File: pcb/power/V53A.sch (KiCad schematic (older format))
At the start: 7 parts

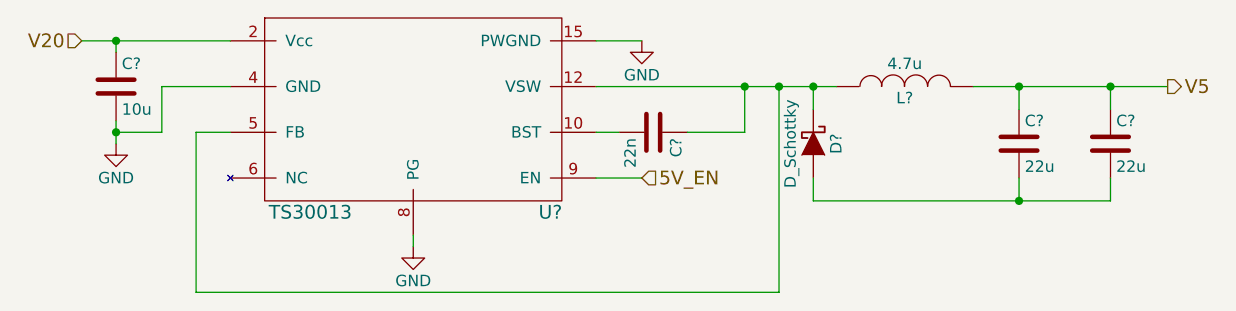
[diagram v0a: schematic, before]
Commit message: Finished almost everything in the schematic. Missing: Interfacing with elmare and the correct power connector for the 20 V power supply.
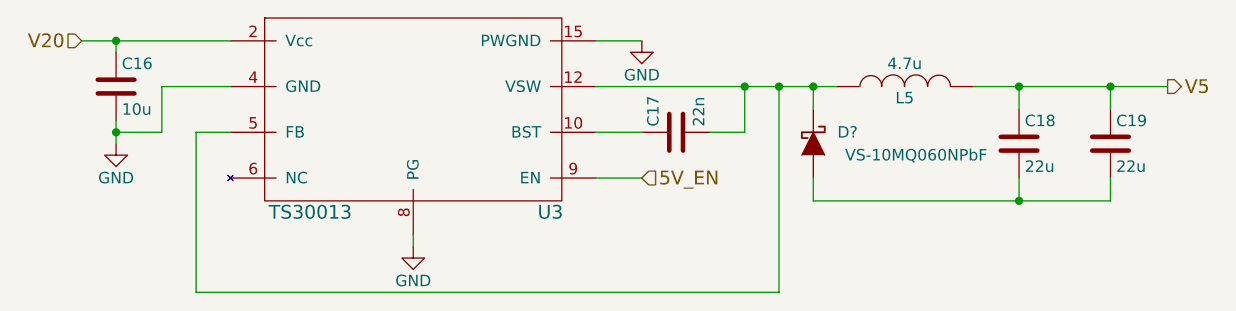
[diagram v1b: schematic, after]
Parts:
- removed C?: 10u, symbol C
- removed C?: 22u, symbol C
- removed C?: 22n, symbol C
- removed D?: D_Schottky, symbol D_Schottky
- added C16: 10u, symbol C
- added C17: 22n, symbol C
- added C19: 22u, symbol C
- added D?: VS-10MQ060NPbF, symbol D_Schottky
- C18: renamed from C?; Digikey (none) -> 1276-1193-1-ND
- L5: renamed from L?; Digikey (none) -> 587-2969-1-ND
- U3: renamed from U?; Digikey (none) -> TS30013-M050QFNRCT-ND
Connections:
- net GND: now also C16.2
- net V20: now also C16.1
- net V5: now also C19.1
- net at L5.1, U3.1 (VSW), U3.12 (VSW)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: now also C17.2, D?.1 (K)
- net at U3.10 (BST): now also C17.1
- net at C18.2: now also C19.2, D?.2 (A)
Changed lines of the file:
@@
 $EndDescr
 $Comp
-L TS30013 U?
+L TS30013 U3
 U 1 1 583B345B
 P 4450 3200
-F 0 "U?" H 5100 2750 60  0000 C CNN
+F 0 "U3" H 5100 2750 60  0000 C CNN
 F 1 "TS30013" H 4050 2750 60  0000 C CNN
 F 2 "" H 4550 3200 60  0000 C CNN
-F 3 "" H 4550 3200 60  0000 C CNN
+F 3 "http://www.semtech.com/images/datasheet/ts30011_12_13.pdf" H 4550 3200 60  0001 C CNN
+F 4 "TS30013-M050QFNRCT-ND" H 4450 3200 60  0001 C CNN "Digikey"
 	1    4450 3200
 	1    0    0    -1
 $EndComp
 $Comp
-L GND #PWR?
+L GND #PWR12
 U 1 1 583B3462
 P 5500 2900
-F 0 "#PWR?" H 5500 2650 50  0001 C CNN
+F 0 "#PWR12" H 5500 2650 50  0001 C CNN
 F 1 "GND" H 5500 2750 50  0000 C CNN
 F 2 "" H 5500 2900 50  0000 C CNN
@@
 $EndComp
 $Comp
-L GND #PWR?
+L GND #PWR10
 U 1 1 583B3468
 P 3200 3350
-F 0 "#PWR?" H 3200 3100 50  0001 C CNN
+F 0 "#PWR10" H 3200 3100 50  0001 C CNN
 F 1 "GND" H 3200 3200 50  0000 C CNN
 F 2 "" H 3200 3350 50  0000 C CNN
@@
 $EndComp
 $Comp
-L C C?
-U 1 1 583B346F
-P 3200 3100
-F 0 "C?" H 3225 3200 50  0000 L CNN
-F 1 "10u" H 3225 3000 50  0000 L CNN
-F 2 "" H 3238 2950 50  0000 C CNN
-F 3 "" H 3200 3100 50  0000 C CNN
-	1    3200 3100
-	1    0    0    -1
-$EndComp
-$Comp
-L C C?
+L C C18
 U 1 1 583B3476
 P 7150 3350
-F 0 "C?" H 7175 3450 50  0000 L CNN
+F 0 "C18" H 7175 3450 50  0000 L CNN
 F 1 "22u" H 7175 3250 50  0000 L CNN
 F 2 "" H 7188 3200 50  0000 C CNN
-F 3 "" H 7150 3350 50  0000 C CNN
+F 3 "http://www.samsungsem.com/kr/support/product-search/mlcc/__icsFiles/afieldfile/2016/08/18/S_CL10A226MQ8NRNC.pdf" H 7150 3350 50  0001 C CNN
+F 4 "1276-1193-1-ND" H 7150 3350 60  0001 C CNN "Digikey"
 	1    7150 3350
 	1    0    0    -1
 $EndComp
 $Comp
-L C C?
-U 1 1 583B347D
-P 7550 3350
-F 0 "C?" H 7575 3450 50  0000 L CNN
-F 1 "22u" H 7575 3250 50  0000 L CNN
-F 2 "" H 7588 3200 50  0000 C CNN
-F 3 "" H 7550 3350 50  0000 C CNN
-	1    7550 3350
-	1    0    0    -1
-$EndComp
-$Comp
-L INDUCTOR L?
+L INDUCTOR L5
 U 1 1 583B3484
 P 6650 3100
-F 0 "L?" V 6600 3100 50  0000 C CNN
+F 0 "L5" V 6600 3100 50  0000 C CNN
 F 1 "4.7u" V 6750 3100 50  0000 C CNN
 F 2 "" H 6650 3100 50  0000 C CNN
-F 3 "" H 6650 3100 50  0000 C CNN
+F 3 "http://www.yuden.co.jp/productdata/catalog/en/wound04_e.pdf" H 6650 3100 50  0001 C CNN
+F 4 "587-2969-1-ND " V 6650 3100 60  0001 C CNN "Digikey"
 	1    6650 3100
 	0    -1   -1   0
 $EndComp
 $Comp
-L D_Schottky D?
-U 1 1 583B348B
-P 6250 3350
-F 0 "D?" H 6250 3450 50  0000 C CNN
-F 1 "D_Schottky" H 6250 3250 50  0000 C CNN
-F 2 "" H 6250 3350 50  0000 C CNN
-F 3 "" H 6250 3350 50  0000 C CNN
-	1    6250 3350
-	0    1    1    0
-$EndComp
-$Comp
-L GND #PWR?
+L GND #PWR11
 U 1 1 583B3492
 P 4500 3800
-F 0 "#PWR?" H 4500 3550 50  0001 C CNN
+F 0 "#PWR11" H 4500 3550 50  0001 C CNN
 F 1 "GND" H 4500 3650 50  0000 C CNN
 F 2 "" H 4500 3800 50  0000 C CNN
@@
 	1    4500 3800
 	1    0    0    -1
-$EndComp
-$Comp
-L C C?
-U 1 1 583B3498
-P 5550 3300
-F 0 "C?" H 5575 3400 50  0000 L CNN
-F 1 "22n" H 5575 3200 50  0000 L CNN
-F 2 "" H 5588 3150 50  0000 C CNN
-F 3 "" H 5550 3300 50  0000 C CNN
-	1    5550 3300
-	0    1    1    0
 $EndComp
 Wire Wire Line
@@
 	5300 2900 5500 2900
 Wire Wire Line
-	5300 3300 5400 3300
-Wire Wire Line
-	5700 3300 5950 3300
+	5300 3300 5500 3300
 Connection ~ 5950 3100
 Wire Wire Line
@@
 Wire Wire Line
 	5500 3500 5300 3500
+$Comp
+L C C16
+U 1 1 583C14BA
+P 3200 3100
+F 0 "C16" H 3225 3200 50  0000 L CNN
+F 1 "10u" H 3225 3000 50  0000 L CNN
+F 2 "" H 3238 2950 50  0000 C CNN
+F 3 "http://search.murata.co.jp/Ceramy/image/img/A01X/G101/ENG/GRT188R61E106ME13-01.pdf" H 3200 3100 50  0001 C CNN
+F 4 "490-12323-1-ND" H 3200 3100 60  0001 C CNN "Digikey"
+	1    3200 3100
+	1    0    0    -1
+$EndComp
+$Comp
+L C C17
+U 1 1 583C19B4
+P 5650 3300
+F 0 "C17" H 5675 3400 50  0000 L CNN
+F 1 "22n" H 5675 3200 50  0000 L CNN
+F 2 "" H 5688 3150 50  0000 C CNN
+F 3 "https://product.tdk.com/info/en/catalog/datasheets/mlcc_highreliability_general_en.pdf" H 5650 3300 50  0001 C CNN
+F 4 "445-8118-1-ND" H 5650 3300 60  0001 C CNN "Digikey"
+	1    5650 3300
+	0    -1   -1   0
+$EndComp
+Wire Wire Line
+	5800 3300 5950 3300
+$Comp
+L C C19
+U 1 1 583C1DEC
+P 7550 3350
+F 0 "C19" H 7575 3450 50  0000 L CNN
+F 1 "22u" H 7575 3250 50  0000 L CNN
+F 2 "" H 7588 3200 50  0000 C CNN
+F 3 "http://www.samsungsem.com/kr/support/product-search/mlcc/__icsFiles/afieldfile/2016/08/18/S_CL10A226MQ8NRNC.pdf" H 7550 3350 50  0001 C CNN
+F 4 "1276-1193-1-ND" H 7550 3350 60  0001 C CNN "Digikey"
+	1    7550 3350
+	1    0    0    -1
+$EndComp
+$Comp
+L D_Schottky D?
+U 1 1 583C3D85
+P 6250 3350
+F 0 "D?" V 6200 3500 50  0000 C CNN
+F 1 "VS-10MQ060NPbF" V 6300 3800 50  0000 C CNN
+F 2 "" H 6250 3350 50  0000 C CNN
+F 3 "http://www.vishay.com/docs/88869/packaging.pdf" H 6250 3350 50  0001 C CNN
+F 4 "10MQ060NPBFCT-ND" V 6300 3950 60  0001 C CNN "Digikey"
+	1    6250 3350
+	0    1    1    0
+$EndComp
 $EndSCHEMATC

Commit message: Almost done with the schematics. Some fine tuning is left.
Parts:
- gave numbers to parts that had none: 1
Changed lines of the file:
@@
 Date "2016-11-27"
 Rev "v1.0"
-Comp ""
+Comp "Uppsala University"
 Comment1 ""
 Comment2 ""
@@
 $EndComp
 $Comp
-L GND #PWR12
+L GND #PWR14
 U 1 1 583B3462
 P 5500 2900
-F 0 "#PWR12" H 5500 2650 50  0001 C CNN
+F 0 "#PWR14" H 5500 2650 50  0001 C CNN
 F 1 "GND" H 5500 2750 50  0000 C CNN
 F 2 "" H 5500 2900 50  0000 C CNN
@@
 $EndComp
 $Comp
-L GND #PWR10
+L GND #PWR12
 U 1 1 583B3468
 P 3200 3350
-F 0 "#PWR10" H 3200 3100 50  0001 C CNN
+F 0 "#PWR12" H 3200 3100 50  0001 C CNN
 F 1 "GND" H 3200 3200 50  0000 C CNN
 F 2 "" H 3200 3350 50  0000 C CNN
@@
 $EndComp
 $Comp
-L GND #PWR11
+L GND #PWR13
 U 1 1 583B3492
 P 4500 3800
-F 0 "#PWR11" H 4500 3550 50  0001 C CNN
+F 0 "#PWR13" H 4500 3550 50  0001 C CNN
 F 1 "GND" H 4500 3650 50  0000 C CNN
 F 2 "" H 4500 3800 50  0000 C CNN
@@
 $EndComp
 $Comp
-L D_Schottky D?
+L D_Schottky D8
 U 1 1 583C3D85
 P 6250 3350
-F 0 "D?" V 6200 3500 50  0000 C CNN
+F 0 "D8" V 6200 3500 50  0000 C CNN
 F 1 "VS-10MQ060NPbF" V 6300 3800 50  0000 C CNN
 F 2 "" H 6250 3350 50  0000 C CNN
